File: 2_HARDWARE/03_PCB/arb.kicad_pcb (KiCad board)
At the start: 4 copper layers, 104.3 x 53.5 mm, 269 parts, among them J1 TYPE-C-31-M-12, J2 SMA, J3 SMA, J4 BNC, J5 PH-00244, SW1 TS-1187A-B-A-B, U1 TLV70333DBV, U10 LMK1C1103PWR, U11 STM32F446ZETx, U12 ICE40UP5K-SG48ITR, U13 93LC56BT-I_OT, U14 FT2232HL, U15 W25Q128JVSIQ, U16 W25Q128JVSIQ, U17 AD9850, U18 AD9744, U19 LM6171, U2 TLV76133DCY, U20 LM6171, U21 TMUX6104, U22 TPL0401B-10, U23 THS3491, U24 ADG1219BRJZ, U25 LM6171, U26 TMUX6104, U3 TLV70333DBV, U4 LM3880MF-1AA, U5 TLV70312DBV, U6 TLV70325DBV, U7 TPS65131RGE, U8 TPD2E001DRL, U9 ADG1219BRJZ, X1 ASE-10.000MHz, X2 ASE-100.000MHz, Y1 32.768k, Y2 12 MHz

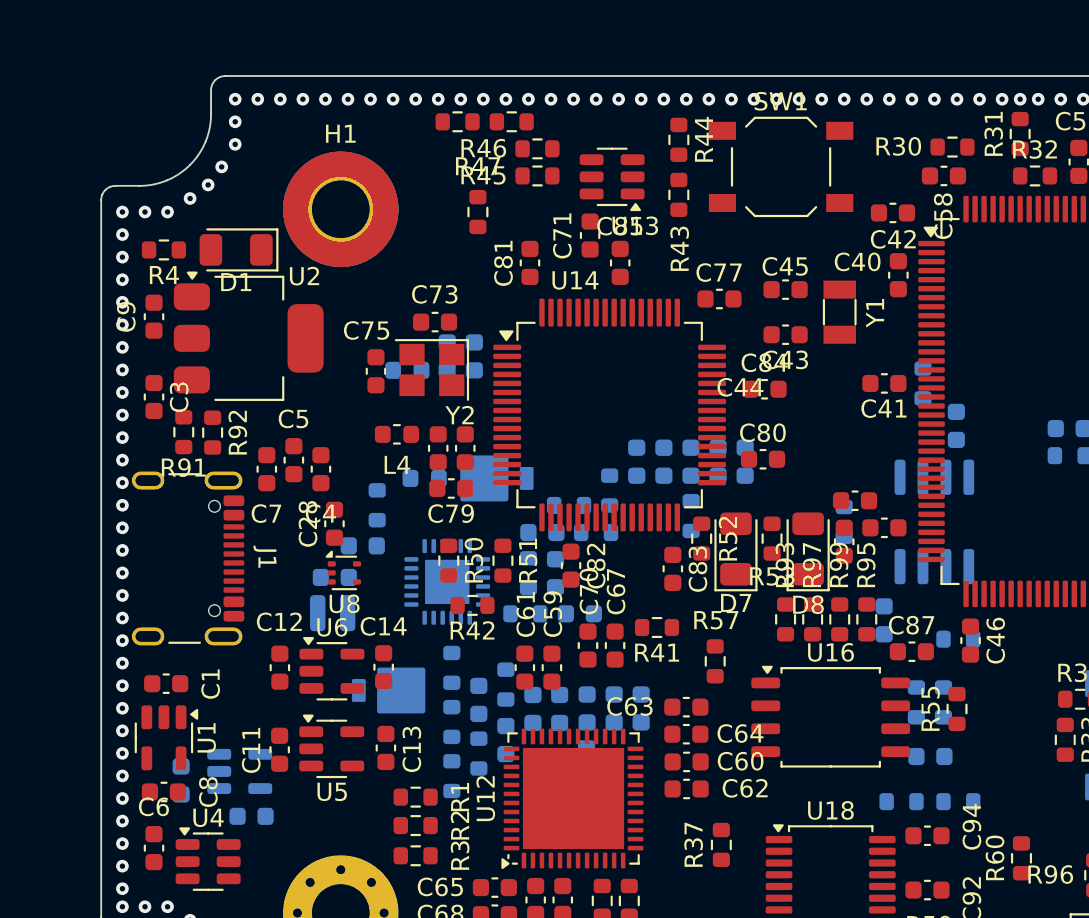
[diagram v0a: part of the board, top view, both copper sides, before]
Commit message: MINORL: Completed 3.3V Regulator Power Planes. Started on FTDI Clock.
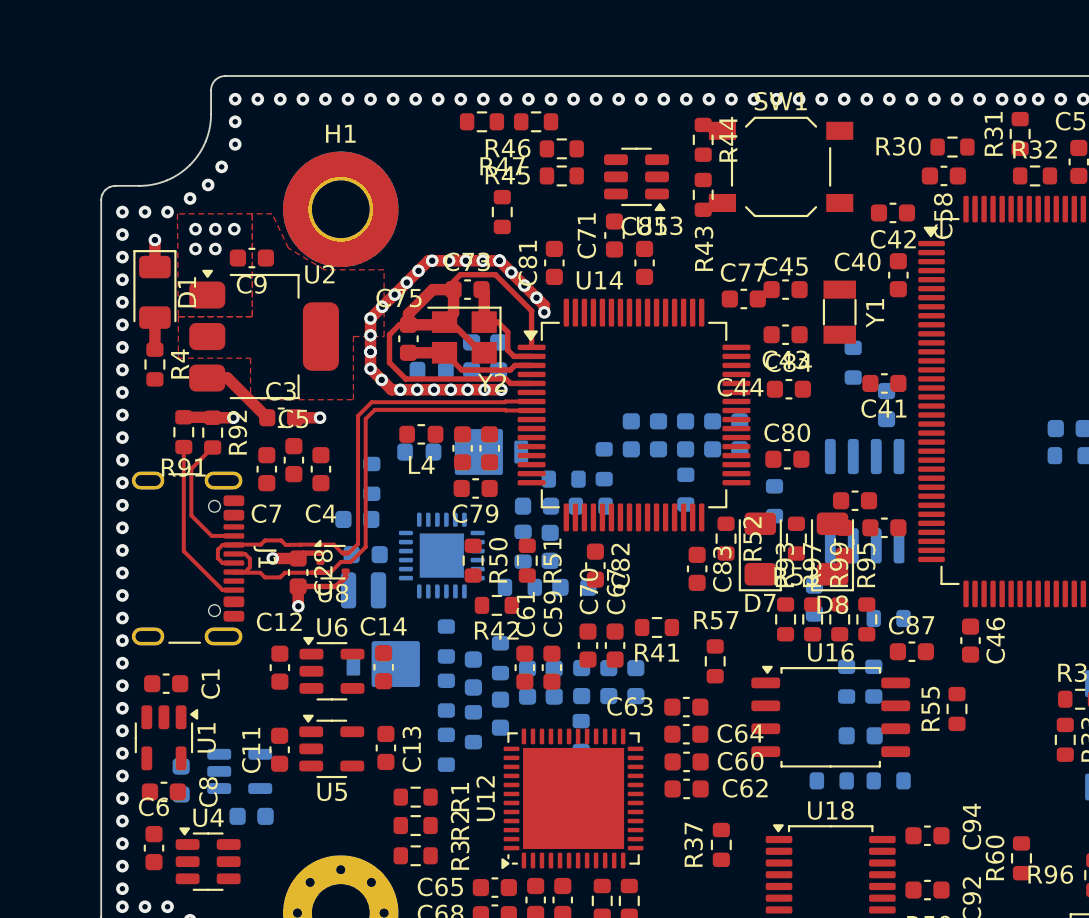
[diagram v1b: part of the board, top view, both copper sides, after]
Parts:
- moved C3 7.14 mm to (105.8, 79.0), turned to 0 degrees
- moved R4 6.37 mm to (98.8, 76.0), turned to -90 degrees
- moved C9 6.32 mm to (104.2, 70.1), turned to 180 degrees
- moved D1 5.08 mm to (98.8, 72.0), turned to -90 degrees
- moved C97 4.03 mm to (139.3, 78.2)
- moved C95 4.03 mm to (137.9, 96.6)
- moved C99 4.03 mm to (135.3, 89.0)
- moved R61 4.03 mm to (136.3, 99.1)
- moved R65 4.03 mm to (137.1, 93.6)
- moved R66 4.03 mm to (138.6, 93.6)
- moved R71 4.03 mm to (133.1, 83.6)
- moved R73 4.03 mm to (137.5, 75.9)
- moved U19 4.03 mm to (138.1, 83.6)
- moved R63 4.03 mm to (139.5, 99.1)
- moved R69 4.03 mm to (139.5, 90.1)
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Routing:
- net GND: track 0.00 -> 62.1 mm, vias 221 -> 257
- net USB_DATA_CONN_FTDI_P: track 0.00 -> 28.1 mm
- net USB_DATA_CONN_FTDI_N: track 0.00 -> 26.8 mm
- net Net-(J1-CC2): track 0.00 -> 9.44 mm
- net Net-(U14-OSCO): track 0.00 -> 7.32 mm
- net Net-(J1-CC1): track 0.00 -> 7.08 mm
- net 5P0V: track 0.00 -> 7.00 mm, vias 0 -> 1
- net Net-(U14-OSCI): track 0.00 -> 6.41 mm
- net Net-(D1-A): track 0.00 -> 1.77 mm
- added copper zone on F.Cu, net 3P3V_D
- added copper zone on F.Cu, net GND

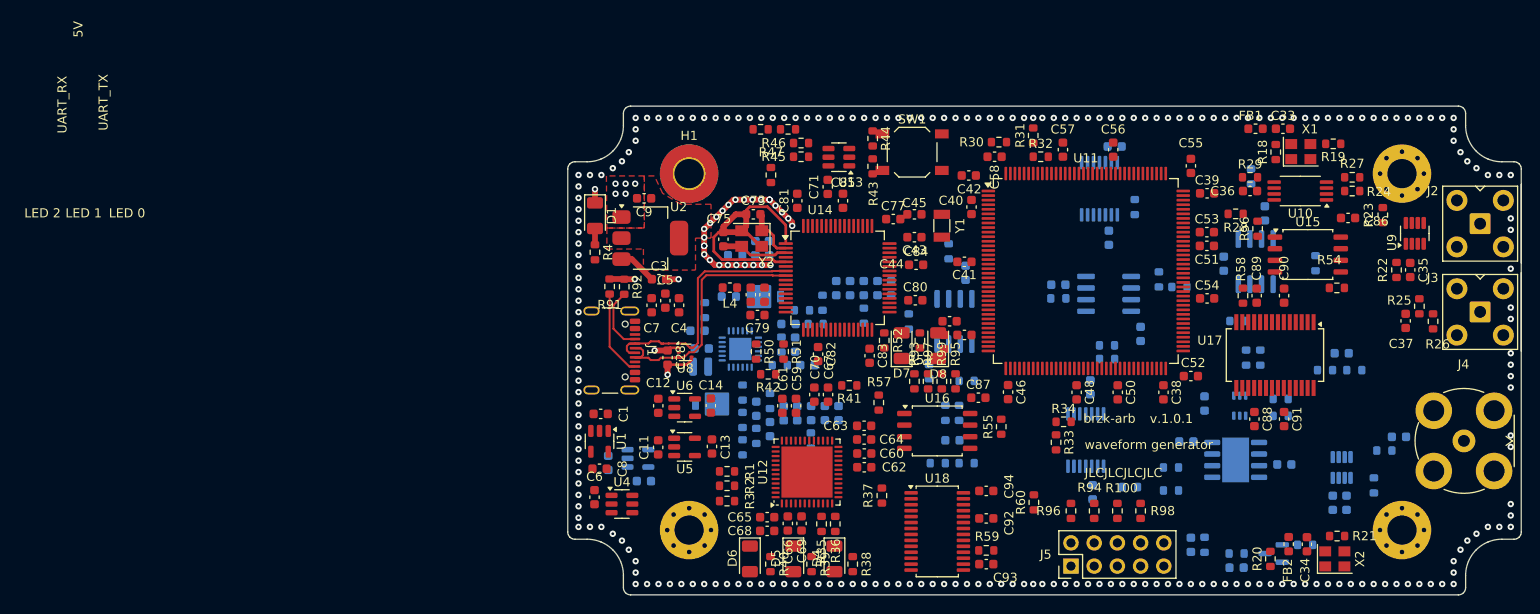
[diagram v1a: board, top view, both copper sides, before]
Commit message: MINOR: Routed (most of) the clocks.
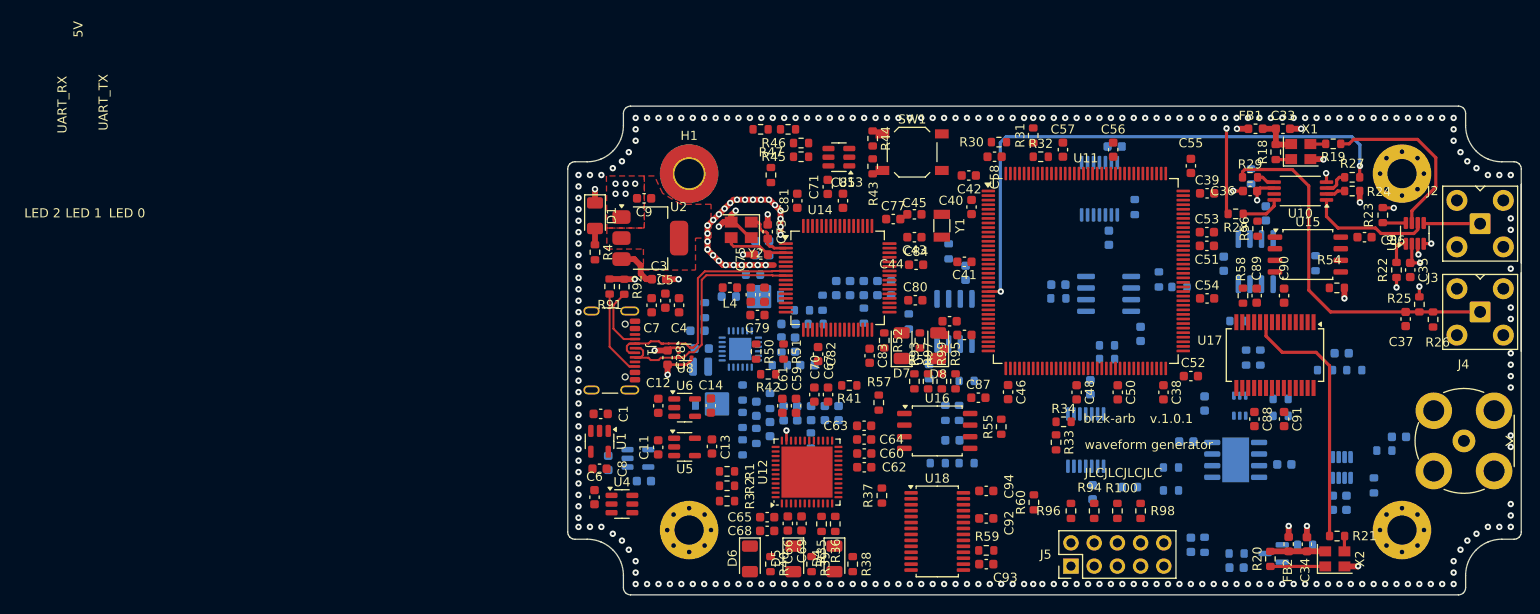
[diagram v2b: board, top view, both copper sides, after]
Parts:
- moved C75 4.43 mm to (117.0, 76.2), turned to 180 degrees
- moved L3 2.89 mm to (116.1, 78.5)
- moved C86 2.77 mm to (183.0, 74.3)
- moved C73 2.47 mm to (117.7, 73.8), turned to 90 degrees
- moved Y2 1.49 mm to (114.8, 73.5)
- moved C37 0.21 mm to (187.5, 83.3)
- moved R25 0.21 mm to (189.0, 81.7)
- moved R26 0.21 mm to (190.5, 83.4)
- moved C98 0.10 mm to (172.2, 71.8)
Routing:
- net CLK_10MHZ_DIST_MCU_3P3: track 0.00 -> 61.2 mm, vias 0 -> 2
- net CLK_10MHZ_DIST_EXT_3P3: track 0.00 -> 39.8 mm
- net CLK_100MHZ_DDS_3P3: track 0.00 -> 28.4 mm
- net Net-(U9-SA): track 0.00 -> 19.7 mm
- net Net-(U10-CLKIN): track 0.00 -> 13.5 mm
- net 3P3V_D: track 0.00 -> 13.3 mm, vias 0 -> 8
- net CLK_10MHZ_DIST_FPGA_3P3: track 0.00 -> 10.5 mm, vias 0 -> 2
- net GND: track 62.1 -> 51.7 mm, vias 257 -> 269
- net CLK_10MHZ_EXT_SW_3P3: track 0.00 -> 6.20 mm
- net Net-(X2-Vdd): track 0.00 -> 6.00 mm
- net GPIO_100M-EN_MCU_100M-OSC_3P3: track 0.00 -> 6.00 mm
- net Net-(X1-Vdd): track 0.00 -> 4.88 mm
- net Net-(U10-Y1): track 0.00 -> 4.41 mm
- net Net-(U9-EN): track 0.00 -> 2.90 mm
- net Net-(U10-Y0): track 0.00 -> 2.78 mm
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
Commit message: MAJOR: Converted PCB from 4 Layer to 6 Layer, updated board stackup, and added new trace constraints. Updated all active traces on PCB to new widths.
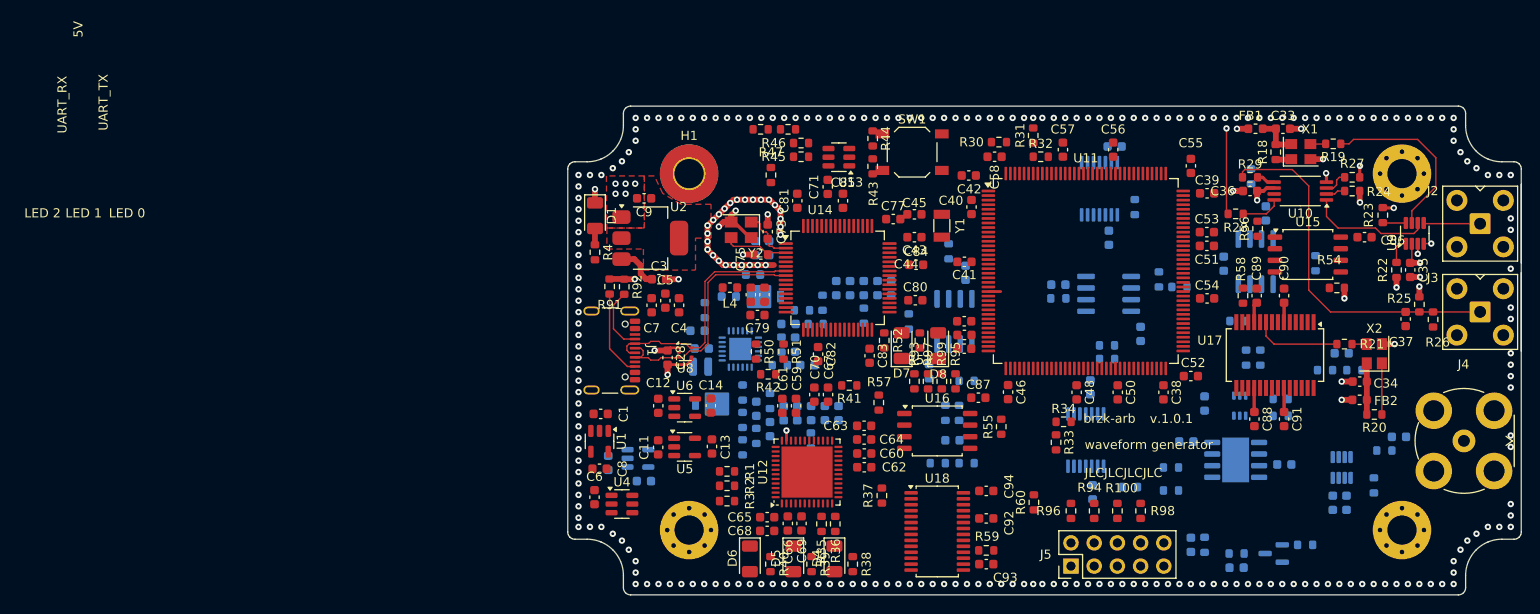
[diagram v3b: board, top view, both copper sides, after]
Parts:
- moved X2 22.9 mm to (184.1, 87.1), turned to 90 degrees
- moved R21 21.0 mm to (180.8, 86.0)
- moved R20 19.5 mm to (184.1, 93.8), turned to 180 degrees
- moved C34 18.7 mm to (182.5, 90.2), turned to 180 degrees
- moved FB2 17.6 mm to (182.5, 92.2), turned to 0 degrees
- moved C49 2.32 mm to (139.2, 86.5), turned to 180 degrees
- moved C44 1.60 mm to (139.2, 83.5)
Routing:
- net CLK_10MHZ_DIST_MCU_3P3: track 61.2 -> 2.62 mm, vias 2 -> 1
- net CLK_100MHZ_DDS_3P3: track 28.4 -> 9.64 mm
- net 3P3V_A: track 0.00 -> 4.87 mm
- net 3P3V_D: track 13.3 -> 18.1 mm
- net GND: track 51.7 -> 52.5 mm, vias 269 -> 270
- added copper zone on In4.Cu, net GND
- removed copper zone on In2.Cu, net GND
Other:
- copper layers 4 -> 6

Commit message: MINOR: Finalized Clock Routing & started on FTDI Chip Routing.
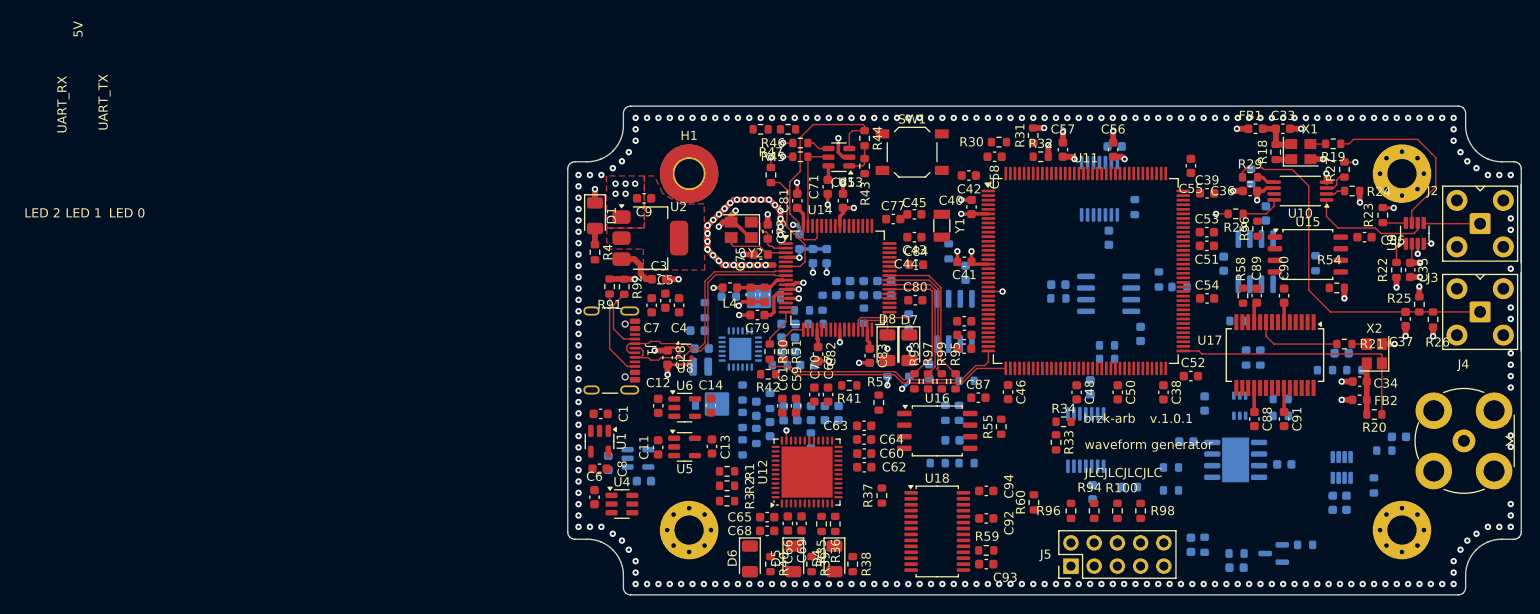
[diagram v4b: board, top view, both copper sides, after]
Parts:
- R52, R53: moved to B.Cu
- moved C72 7.85 mm to (124.2, 76.4), turned to -90 degrees
- moved L3 6.22 mm to (121.2, 74.8), turned to -90 degrees
- moved D8 5.55 mm to (130.8, 86.5), turned to -90 degrees
- moved C76 4.88 mm to (122.7, 76.4), turned to -90 degrees
- moved R53 4.71 mm to (130.8, 88.8)
- moved R52 4.14 mm to (133.2, 88.8)
- moved R50 1.49 mm to (117.9, 86.9)
- moved R27 1.20 mm to (180.8, 67.0), turned to -90 degrees
- moved R44 0.89 mm to (128.3, 63.5)
- moved R43 0.89 mm to (128.3, 66.6)
- moved D7 0.88 mm to (133.2, 86.5), turned to -90 degrees
- moved R45 0.07 mm to (121.3, 65.5)
- moved R46 0.07 mm to (121.3, 64.0)
- turned C55 to -90 degrees
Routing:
- net CLK_10MHZ_DIST_FPGA_3P3: track 10.5 -> 68.1 mm
- net CLK_10MHZ_DIST_MCU_3P3: track 2.62 -> 54.8 mm, vias 1 -> 2
- net GND: track 52.5 -> 83.2 mm, vias 270 -> 292
- net UART_FTDITX_MCURX_3P3: track 0.00 -> 27.9 mm
- net Net-(U13-DI): track 0.00 -> 26.7 mm
- net 3P3V_D: track 18.1 -> 44.5 mm, vias 8 -> 20
- net UART_MCUTX_FTDIRX_3P3: track 0.00 -> 25.4 mm
- net GPIO_100M-EN_MCU_100M-OSC_3P3: track 5.60 -> 28.4 mm
- net JTAG_FTDI_TMS_3P3: track 0.00 -> 16.3 mm
- net JTAG_FTDI_TDO_3P3: track 0.00 -> 15.3 mm
- net JTAG_FTDI_TDI_3P3: track 0.00 -> 14.7 mm
- net JTAG_FTDI_TCK_3P3: track 0.00 -> 14.6 mm
- net Net-(U14-REF): track 0.00 -> 13.1 mm
- net Net-(U13-CS): track 0.00 -> 9.88 mm
- net GPIO_UART_RXLED_FTDI_L: track 0.00 -> 8.41 mm
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
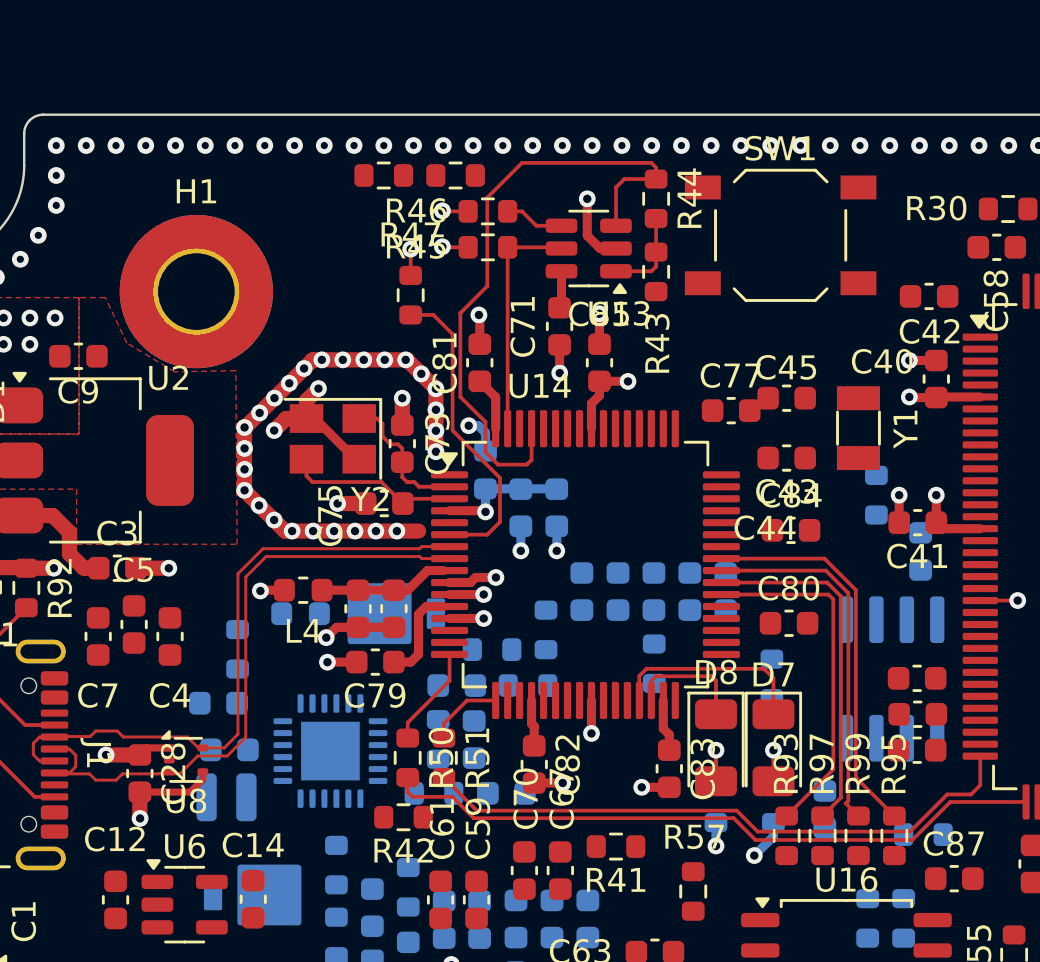
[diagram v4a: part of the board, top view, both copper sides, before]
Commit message: MINOR: Finalized FTDI Chip Routing.
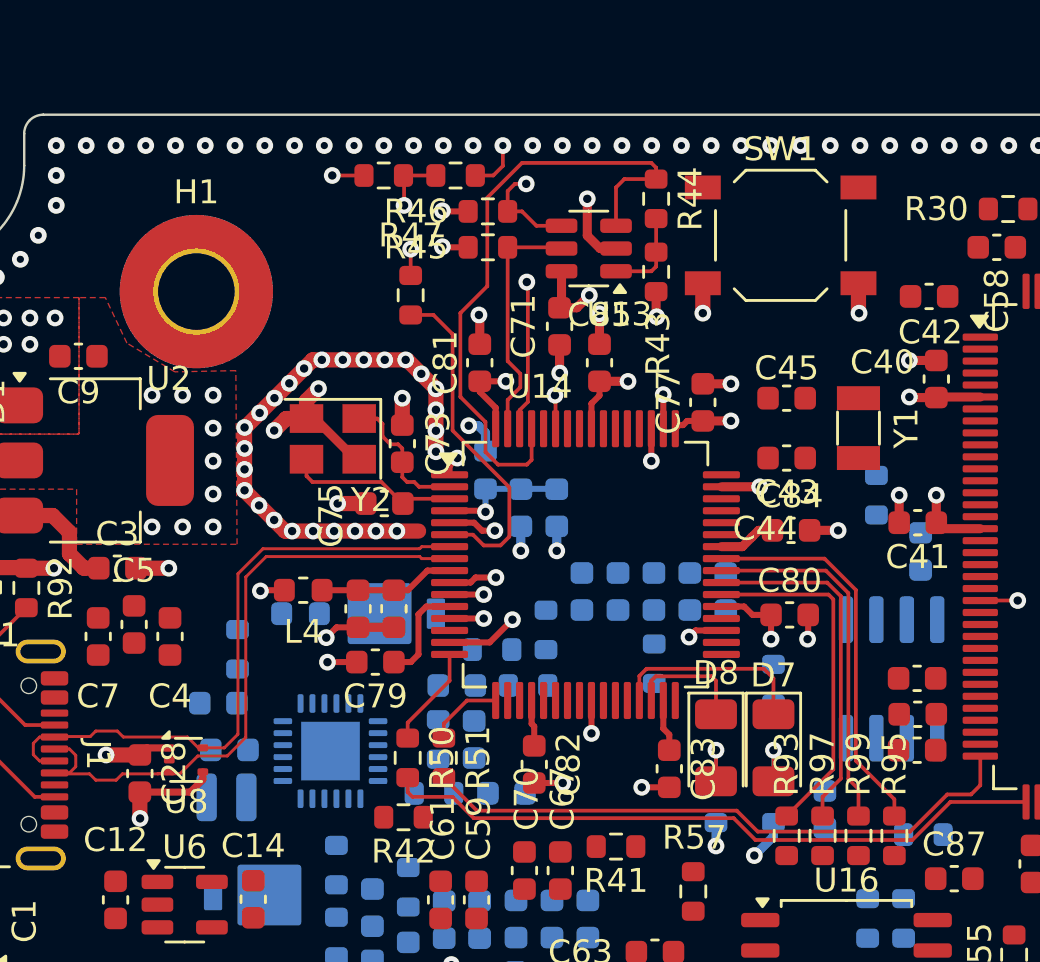
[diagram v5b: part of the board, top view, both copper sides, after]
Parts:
- moved C77 1.23 mm to (130.2, 72.0), turned to 90 degrees
- moved C80 0.35 mm to (133.9, 80.9)
- moved R71 0.23 mm to (133.2, 83.8)
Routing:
- net GND: track 83.2 -> 101.4 mm, vias 292 -> 303
- net Net-(U14-BCBUS7): track 0.00 -> 17.1 mm, vias 0 -> 2
- net Net-(U13-CLK): track 2.50 -> 14.6 mm, vias 0 -> 2
- net 1P8V_D: track 6.26 -> 13.1 mm, vias 0 -> 3
- net 3P3V_D: track 44.5 -> 50.9 mm, vias 20 -> 32
- net 5P0V: track 7.53 -> 8.85 mm, vias 1 -> 2
- net Net-(U14-REF): track 13.1 -> 14.4 mm
